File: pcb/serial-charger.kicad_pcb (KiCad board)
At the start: 2 copper layers, 25.5 x 13 mm, 22 parts, among them IC1 CH340G, IC2 TP4056, P1 CONN_01X01, P2 USB_OTG, P3 CONN_01X05, P4 CONN_01X01, x1 xtal_osc

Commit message: disabled thermal shutoff from charger
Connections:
- IC2 pad 1: Net-(IC2-Pad1) -> GND
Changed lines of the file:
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@@
 (kicad_pcb (version 4) (host pcbnew 4.0.2+dfsg1-stable)
   (general
-    (links 46)
+    (links 47)
     (no_connects 0)
-    (area 112.075 72.275 149.875001 91.269)
+    (area 114.949999 76.949999 140.550001 90.050001)
     (thickness 1.6)
     (drawings 16)
@@
     (zones 0)
     (modules 22)
-    (nets 25)
+    (nets 24)
   )
   (page A4)
@@
   )
   (setup
-    (last_trace_width 0.3)
+    (last_trace_width 0.25)
     (user_trace_width 0.2)
     (user_trace_width 0.3)
@@
   (net 21 "Net-(IC1-Pad15)")
   (net 22 "Net-(IC2-Pad6)")
-  (net 23 "Net-(IC2-Pad1)")
-  (net 24 "Net-(P2-Pad4)")
+  (net 23 "Net-(P2-Pad4)")
   (net_class Default "This is the default net class."
     (clearance 0.1524)
@@
     (add_net "Net-(IC1-Pad15)")
     (add_net "Net-(IC1-Pad9)")
-    (add_net "Net-(IC2-Pad1)")
     (add_net "Net-(IC2-Pad2)")
     (add_net "Net-(IC2-Pad6)")
@@
       (net 5 D+))
     (pad 4 smd rect (at 0.6491 -1.56254) (size 1.35 0.4) (layers F.Cu F.Paste F.Mask)
-      (net 24 "Net-(P2-Pad4)"))
+      (net 23 "Net-(P2-Pad4)"))
     (pad 5 smd rect (at 1.2991 -1.56254) (size 1.35 0.4) (layers F.Cu F.Paste F.Mask)
       (net 2 GND))
@@
       (net 15 "Net-(IC2-Pad2)"))
     (pad 1 smd rect (at -1.905 3.175 270) (size 0.508 1.143) (layers F.Cu F.Paste F.Mask)
-      (net 23 "Net-(IC2-Pad1)"))
+      (net 2 GND))
     (model SMD_Packages.3dshapes/SOIC-8-N.wrl
       (at (xyz 0 0 0))

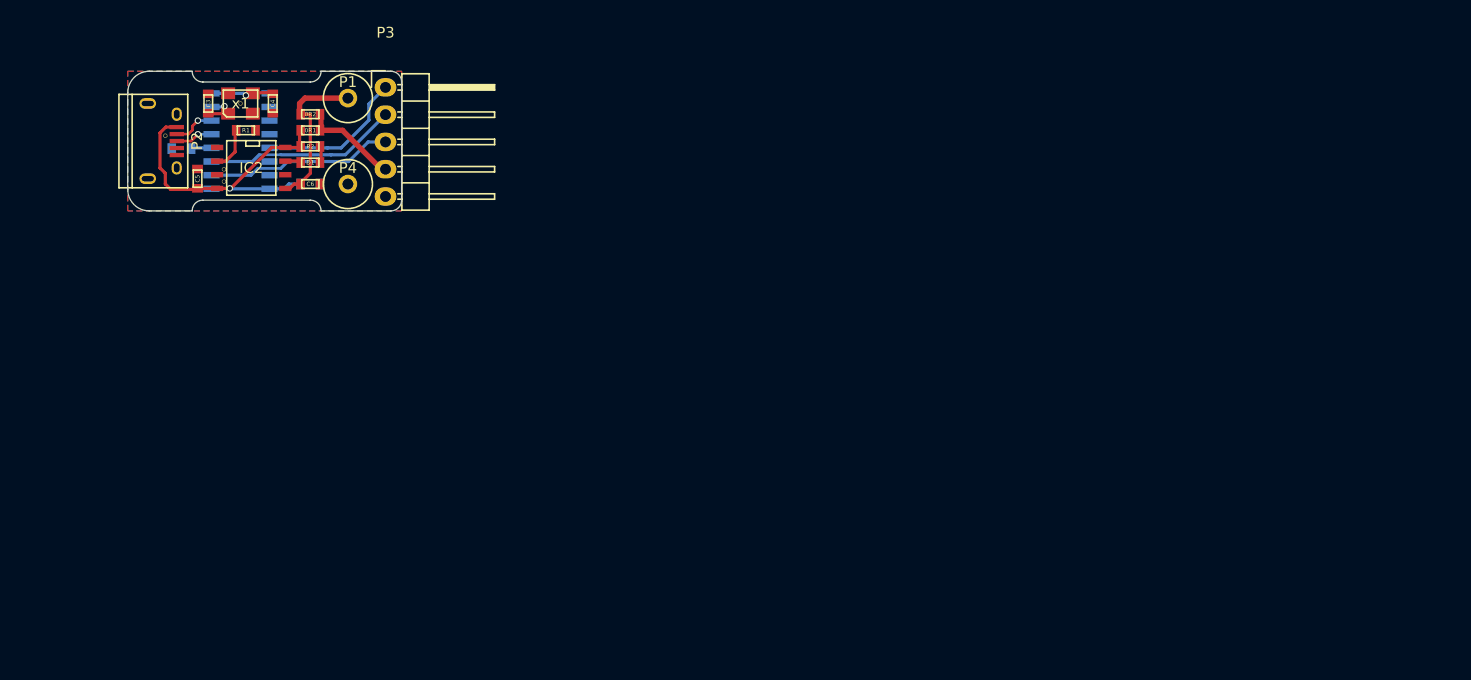
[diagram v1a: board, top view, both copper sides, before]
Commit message: partyhat edition, with built in avr and li-ion holder
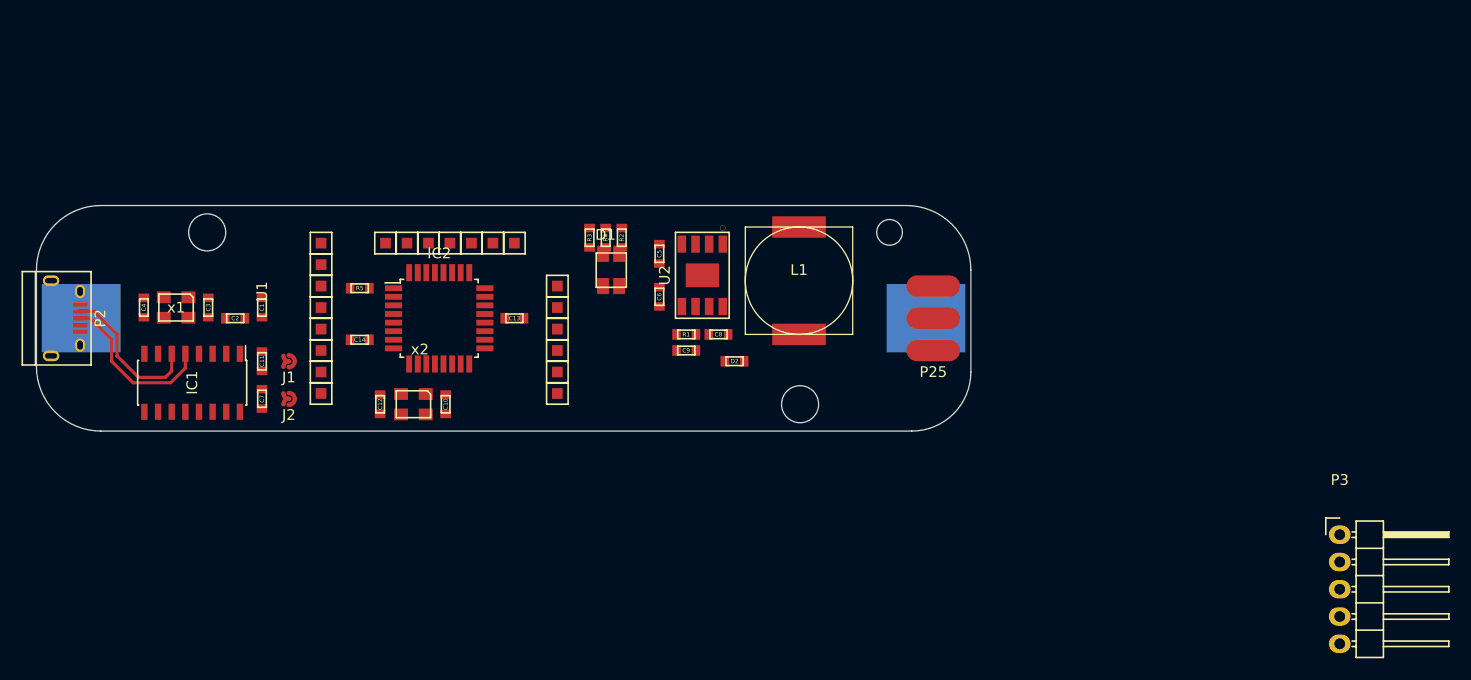
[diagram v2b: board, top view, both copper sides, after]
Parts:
- removed 0R1, 0R2: 0R, netl:SMD_0603
- removed REF** (x4): via, netl:via
- added C10: C, netl:SMD_0603, F.Cu at (144.6, 108.0)
- added C11: C, netl:SMD_0603, F.Cu at (127.5, 104.0)
- added C12: C, netl:SMD_0603, F.Cu at (138.5, 108.0)
- added C13: C, netl:SMD_0603, F.Cu at (151.0, 100.0)
- added C14: C, netl:SMD_0603, F.Cu at (136.6, 102.0)
- added C7: 10u, netl:SMD_0603, F.Cu at (127.5, 107.5)
- added C8: C, netl:SMD_0603, F.Cu at (170.0, 101.5)
- added C9: 47uF, netl:SMD_0603, F.Cu at (167.0, 103.0)
- added D2: D, netl:SMD_0603, F.Cu at (171.5, 104.0)
- added J1: jumper, netl:Jumper, F.Cu at (130.0, 104.0)
- added J2: jumper, netl:Jumper, F.Cu at (130.0, 107.5)
- added L1: INDUCTOR, Inductors:SELF-WE-PD-XXL, F.Cu at (177.5, 96.5)
- added P10: CONNECTOR, netl:1Pin_small, F.Cu at (151.0, 93.0)
- added P11: CONNECTOR, netl:1Pin_small, F.Cu at (149.0, 93.0)
- added P12: CONNECTOR, netl:1Pin_small, F.Cu at (147.0, 93.0)
- added P13: CONNECTOR, netl:1Pin_small, F.Cu at (145.0, 93.0)
- added P14: CONNECTOR, netl:1Pin_small, F.Cu at (143.0, 93.0)
- added P15: CONNECTOR, netl:1Pin_small, F.Cu at (141.0, 93.0)
- added P16: CONNECTOR, netl:1Pin_small, F.Cu at (139.0, 93.0)
- added P17: CONNECTOR, netl:1Pin_small, F.Cu at (133.0, 95.0)
- added P18: CONNECTOR, netl:1Pin_small, F.Cu at (133.0, 93.0)
- added P19: CONNECTOR, netl:1Pin_small, F.Cu at (133.0, 97.0)
- added P20: CONNECTOR, netl:1Pin_small, F.Cu at (133.0, 99.0)
- added P21: CONNECTOR, netl:1Pin_small, F.Cu at (133.0, 101.0)
- added P22: CONNECTOR, netl:1Pin_small, F.Cu at (133.0, 103.0)
- added P23: CONNECTOR, netl:1Pin_small, F.Cu at (133.0, 105.0)
- added P24: CONNECTOR, netl:1Pin_small, F.Cu at (133.0, 107.0)
- added P25: CONN_01X03, netl:SM_3_WIRE, F.Cu at (190.0, 100.0)
- added P5: CONNECTOR, netl:1Pin_small, F.Cu at (155.0, 105.0)
- added P6: CONNECTOR, netl:1Pin_small, F.Cu at (155.0, 103.0)
- added P7: CONNECTOR, netl:1Pin_small, F.Cu at (155.0, 101.0)
- added P8: CONNECTOR, netl:1Pin_small, F.Cu at (155.0, 99.0)
- added P9: CONNECTOR, netl:1Pin_small, F.Cu at (155.0, 97.0)
- added R3: 1k, netl:SMD_0603, F.Cu at (158.0, 92.5)
- added R4: 1k, netl:SMD_0603, F.Cu at (159.5, 92.5)
- added R5: R, netl:SMD_0603, F.Cu at (136.6, 97.2)
- added U1: XC6206, TO_SOT_Packages_SMD:SOT-23, F.Cu at (125.5, 97.5)
- added U2: FM6316FE, netl:ESOP-8, F.Cu at (168.5, 96.0)
- added x2: xtal_osc, netl:SM_3225, F.Cu at (141.6, 108.0)
- C1, C2, IC1: moved to F.Cu
- D1: value LED -> RGB_LED; footprint netl:SMD_0603 -> netl:RGB_LED
- IC2: value TP4056 -> ATMEGA168-P; footprint SMD_Packages:SOIC-8-N -> Housings_QFP:TQFP-32_7x7mm_Pitch0.8mm
- P1: value CONN_01X01 -> CONN_01X02; footprint Connect:1pin -> netl:18560; moved to B.Cu
- P4: value CONN_01X01 -> CONNECTOR; footprint Connect:1pin -> netl:1Pin_small
- moved P3 98.1 mm to (227.8, 120.1)
- moved R1 45.2 mm to (167.0, 101.5)
- moved C5 43.6 mm to (164.5, 94.0), turned to 270 degrees
- moved C6 34.2 mm to (164.5, 98.0), turned to 90 degrees
- moved R2 30.2 mm to (161.0, 92.5), turned to 270 degrees
- moved D1 29.7 mm to (160.0, 95.5), turned to 180 degrees
- moved P4 27.6 mm to (155.0, 107.0), turned to 90 degrees
- moved P1 25.1 mm to (150.0, 100.0)
- moved IC1 22.9 mm to (121.0, 106.0), turned to 270 degrees
- moved C4 22.5 mm to (116.5, 99.0), turned to 90 degrees
- moved IC2 22.4 mm to (144.0, 100.0), turned to 0 degrees
- moved x1 19.9 mm to (119.5, 99.0), turned to 0 degrees
- moved C3 19.0 mm to (122.5, 99.0), turned to 270 degrees
- moved P2 18.8 mm to (109.0, 100.0)
- moved C2 16.6 mm to (125.0, 100.0), turned to 180 degrees
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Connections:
- IC1 pad 16: V_USB -> V_SER
- IC2 pad 1: GND -> /avr/~RESET
- IC2 pad 2: Net-(IC2-Pad2) -> TX
- IC2 pad 3: GND -> RX
- IC2 pad 4: V_USB -> Net-(IC2-Pad4)
- IC2 pad 5: VBat -> Net-(IC2-Pad5)
- IC2 pad 7: Net-(D1-Pad1) -> 5V
- IC2 pad 8: V_USB -> GND
- P1 pad 1: VBat -> GND
- P3 pad 4: U_OUT -> V_MCU
- P4 pad 1: GND -> /avr/LED_SRIP
- R1 pad 1: GND -> Net-(R1-Pad1)
- R1 pad 2: Net-(IC2-Pad2) -> GND
- R2 pad 1: Net-(D1-Pad2) -> ~chrg
- R2 pad 2: V_USB -> Net-(D1-Pad1)
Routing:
- net V_USB: track 29.6 -> 0.00 mm, vias 1 -> 0
- net RX: track 18.2 -> 0.00 mm
- net TX: track 17.5 -> 0.00 mm
- net VBat: track 15.1 -> 0.00 mm
- net ~DTR: track 14.0 -> 0.00 mm
- net D+: track 3.50 -> 15.4 mm, vias 1 -> 0
- net D-: track 3.98 -> 14.1 mm, vias 1 -> 0
- net U_OUT: track 8.50 -> 0.00 mm
- net Net-(C4-Pad1): track 5.87 -> 0.00 mm, vias 1 -> 0
- net Net-(IC2-Pad2): track 4.03 -> 0.00 mm
- net Net-(C3-Pad1): track 3.90 -> 0.00 mm, vias 1 -> 0
- net 3V3: track 1.83 -> 0.00 mm
- net Net-(D1-Pad2): track 1.50 -> 0.00 mm
- net Net-(D1-Pad1): track 1.38 -> 0.00 mm
- net GND: track 0.54 -> 0.00 mm
- removed copper zone on B.Cu, net GND
- removed copper zone on F.Cu, net GND
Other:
- board size 25.5 x 13 mm -> 87 x 21 mm

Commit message: layout mostly done
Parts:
- added REF**: via, netl:via, F.Cu at (173.5, 94.8)
- added REF**: via, netl:via, F.Cu at (169.5, 95.5)
- added REF**: via, netl:via, F.Cu at (168.5, 95.5)
- added REF**: via, netl:via, F.Cu at (168.5, 96.5)
- added REF**: via, netl:via, F.Cu at (169.5, 96.5)
- added REF**: via, netl:via, F.Cu at (167.5, 96.5)
- added REF**: via, netl:via, F.Cu at (167.5, 95.5)
- added REF**: via, netl:via, F.Cu at (173.5, 93.8)
- added REF**: via, netl:via, F.Cu at (173.5, 92.8)
- added REF**: via, netl:via, F.Cu at (176.5, 92.8)
- added REF**: via, netl:via, F.Cu at (176.5, 93.8)
- added REF**: via, netl:via, F.Cu at (176.5, 94.8)
- added REF**: via, netl:via, F.Cu at (179.5, 93.8)
- added REF**: via, netl:via, F.Cu at (179.5, 94.8)
- added REF**: via, netl:via, F.Cu at (179.5, 92.8)
- D2: footprint netl:SMD_0603 -> netl:DO-214AC
- L1: footprint Inductors:SELF-WE-PD-XXL -> netl:7x7_Inductor
- P3: value CONN_01X05 -> CONN_01X04; footprint Pin_Headers:Pin_Header_Angled_1x05 -> netl:JST-2mm_4Pin
- moved P3 45.1 mm to (187.5, 100.0), turned to 270 degrees
- moved R3 11.6 mm to (159.2, 104.0), turned to 90 degrees
- moved R5 6.85 mm to (140.0, 91.2), turned to 180 degrees
- moved D2 5.39 mm to (176.5, 102.0)
- moved D1 4.50 mm to (160.0, 100.0)
- moved R2 2.50 mm to (163.0, 94.0)
- moved R4 2.50 mm to (161.5, 94.0)
- moved L1 1.25 mm to (176.5, 95.8), turned to 0 degrees
- moved C10 0.51 mm to (144.5, 107.5)
- moved x2 0.51 mm to (141.5, 107.5)
- moved C12 0.50 mm to (138.5, 107.5)
- moved C13 0.50 mm to (151.5, 100.0)
- turned J1 to 180 degrees
- turned J2 to 180 degrees
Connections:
- IC1 pad 10: Net-(IC1-Pad10) -> (no net)
- IC1 pad 11: Net-(IC1-Pad11) -> (no net)
- IC1 pad 12: Net-(IC1-Pad12) -> (no net)
- IC1 pad 14: Net-(IC1-Pad14) -> (no net)
- IC1 pad 15: Net-(IC1-Pad15) -> (no net)
- IC1 pad 9: Net-(IC1-Pad9) -> (no net)
- P2 pad 4: Net-(P2-Pad4) -> (no net)
- P3 pad 1: ~DTR -> GND
- P3 pad 2: RX -> TX
- P3 pad 3: TX -> RX
- P3 pad 4: V_MCU -> 5V
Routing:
- net RX: track 0.00 -> 82.6 mm, vias 0 -> 2
- net 5V: track 0.00 -> 79.6 mm, vias 0 -> 4
- net TX: track 0.00 -> 77.4 mm, vias 0 -> 4
- net V_USB: track 0.00 -> 77.2 mm, vias 0 -> 6
- net /avr/LED_SRIP: track 0.00 -> 53.5 mm
- net GND: track 0.00 -> 31.8 mm, vias 0 -> 12
- net /avr/~RESET: track 0.00 -> 26.9 mm, vias 0 -> 2
- net 3V3: track 0.00 -> 23.4 mm
- net VBat: track 0.00 -> 17.5 mm, vias 0 -> 2
- net Net-(IC2-Pad13): track 0.00 -> 15.2 mm, vias 0 -> 2
- net Net-(IC2-Pad12): track 0.00 -> 13.5 mm, vias 0 -> 2
- net Net-(IC2-Pad11): track 0.00 -> 12.2 mm, vias 0 -> 2
- net ~stby: track 0.00 -> 10.5 mm
- net Net-(IC2-Pad19): track 0.00 -> 10.3 mm
- net Net-(IC2-Pad15): track 0.00 -> 10.2 mm
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- added copper zone on F.Cu, net 5V
- added copper zone on B.Cu, net GND
- added copper zone on F.Cu, net Net-(C8-Pad2)
- added copper zone on B.Cu, net VBat
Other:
- outline, holes or cut-outs redrawn
- board text added: "Hi there!"

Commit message: first prototype
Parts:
- added C9: 47uF, Capacitors_SMD:C_1206, F.Cu at (167.0, 104.8)
- added G***: LOGO, netl:LOGO_127mm_Bottom_SS, F.Cu at (160.5, 100.0)
- added REF**: via, netl:via, F.Cu at (148.8, 108.2)
- D2: footprint netl:DO-214AC -> netl:SMD_0603
- moved U1 1.80 mm to (126.5, 99.0)
- moved C1 1.50 mm to (129.0, 99.0)
- moved C2 1.41 mm to (124.0, 99.0), turned to 270 degrees
- moved D2 1.00 mm to (176.5, 101.0)
- turned J1 to 0 degrees
- turned J2 to 0 degrees
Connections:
- IC1 pad 10: (no net) -> Net-(IC1-Pad10)
- IC1 pad 11: (no net) -> Net-(IC1-Pad11)
- IC1 pad 12: (no net) -> Net-(IC1-Pad12)
- IC1 pad 14: (no net) -> Net-(IC1-Pad14)
- IC1 pad 15: (no net) -> Net-(IC1-Pad15)
- IC1 pad 9: (no net) -> Net-(IC1-Pad9)
- P2 pad 4: (no net) -> Net-(P2-Pad4)
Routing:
- net GND: track 31.8 -> 53.5 mm, vias 12 -> 16
- net VBat: track 17.5 -> 9.39 mm, vias 2 -> 1
- net 3V3: track 23.4 -> 17.0 mm
- net 5V: track 79.6 -> 76.1 mm
- net Net-(D1-Pad2): track 7.02 -> 3.81 mm
- net /avr/~RESET: track 26.9 -> 29.7 mm
- net TX: track 77.4 -> 78.4 mm
- net RX: track 82.6 -> 83.6 mm
- net V_USB: track 77.2 -> 76.2 mm, vias 6 -> 5
- net V_SER: track 6.90 -> 7.69 mm
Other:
- board text added: "3.3V"
- board text added: "5V"
- board text added: "GND"
- board text added: "PORTB"
- board text added: "PORTC"
- board text added: "PORTD"
